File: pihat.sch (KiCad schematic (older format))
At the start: 1 part, among them J1 Raspberry_Pi_2_3

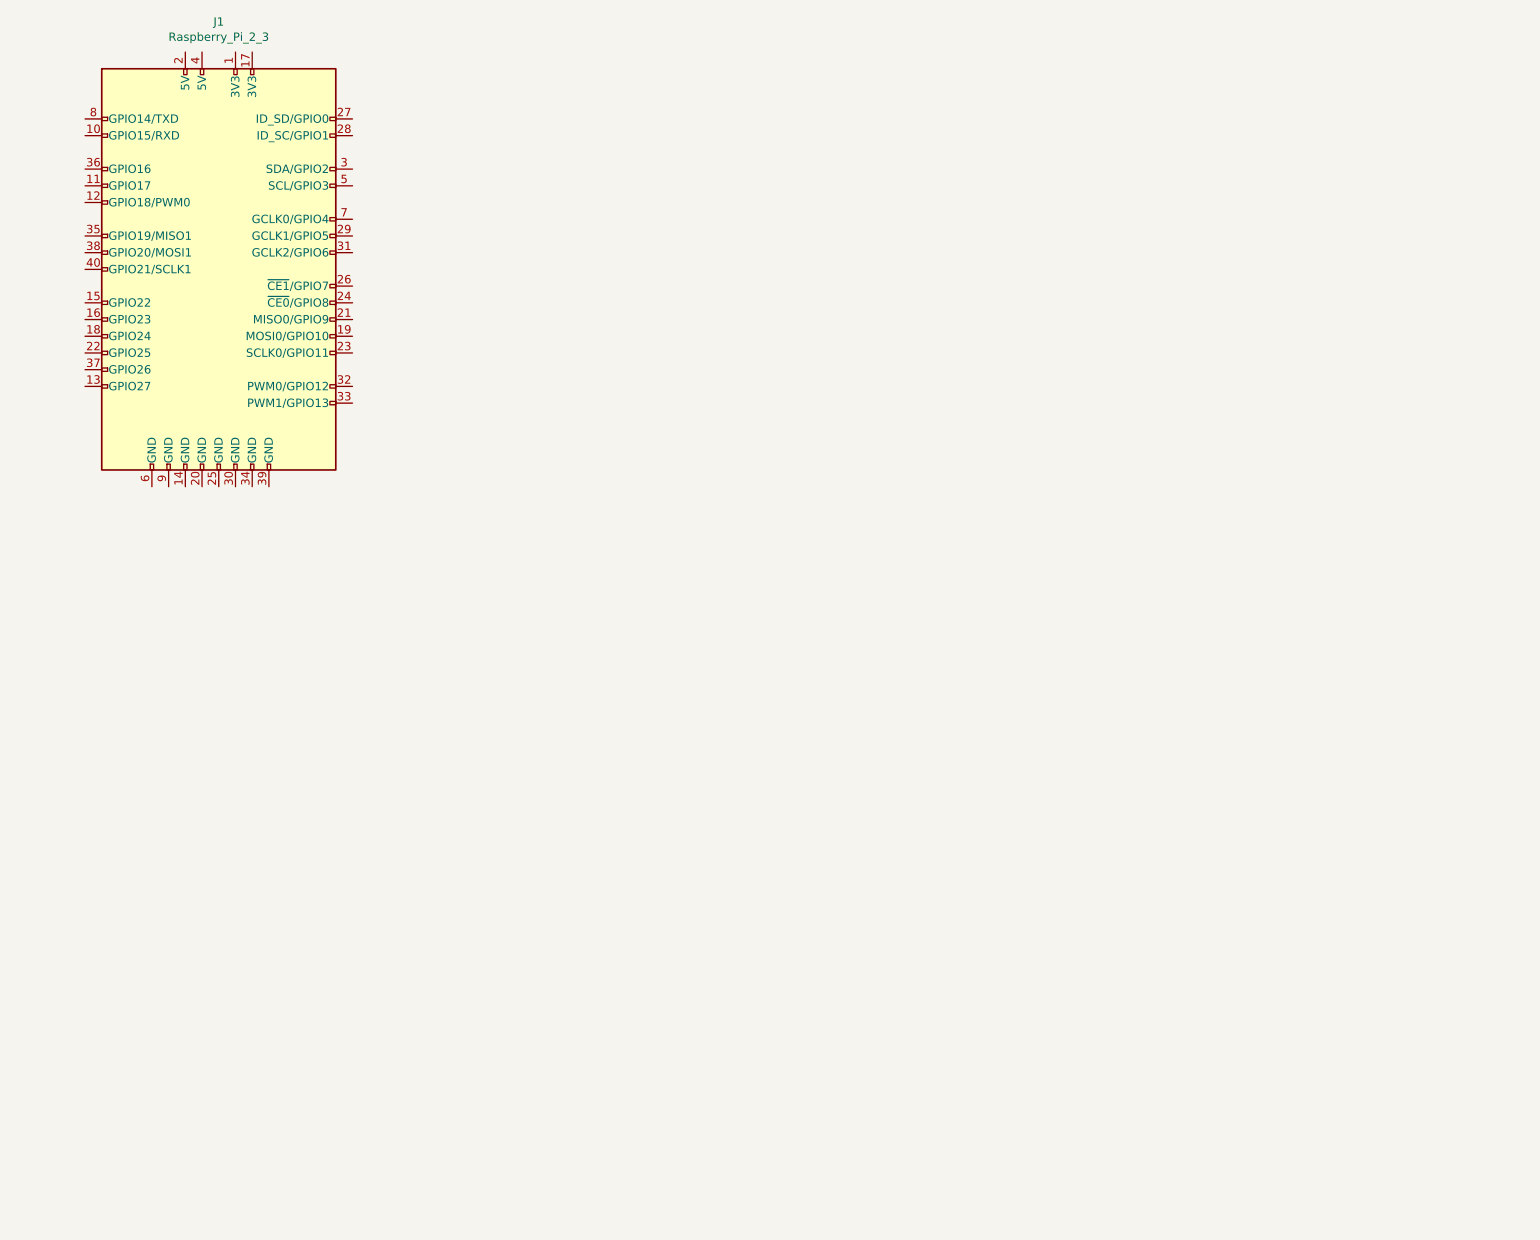
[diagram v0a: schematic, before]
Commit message: Add initial schematic for hat
This adds a USB<->UART converter and a 1-wire bus master, as well as
screw connectors for heating elements and sensors.
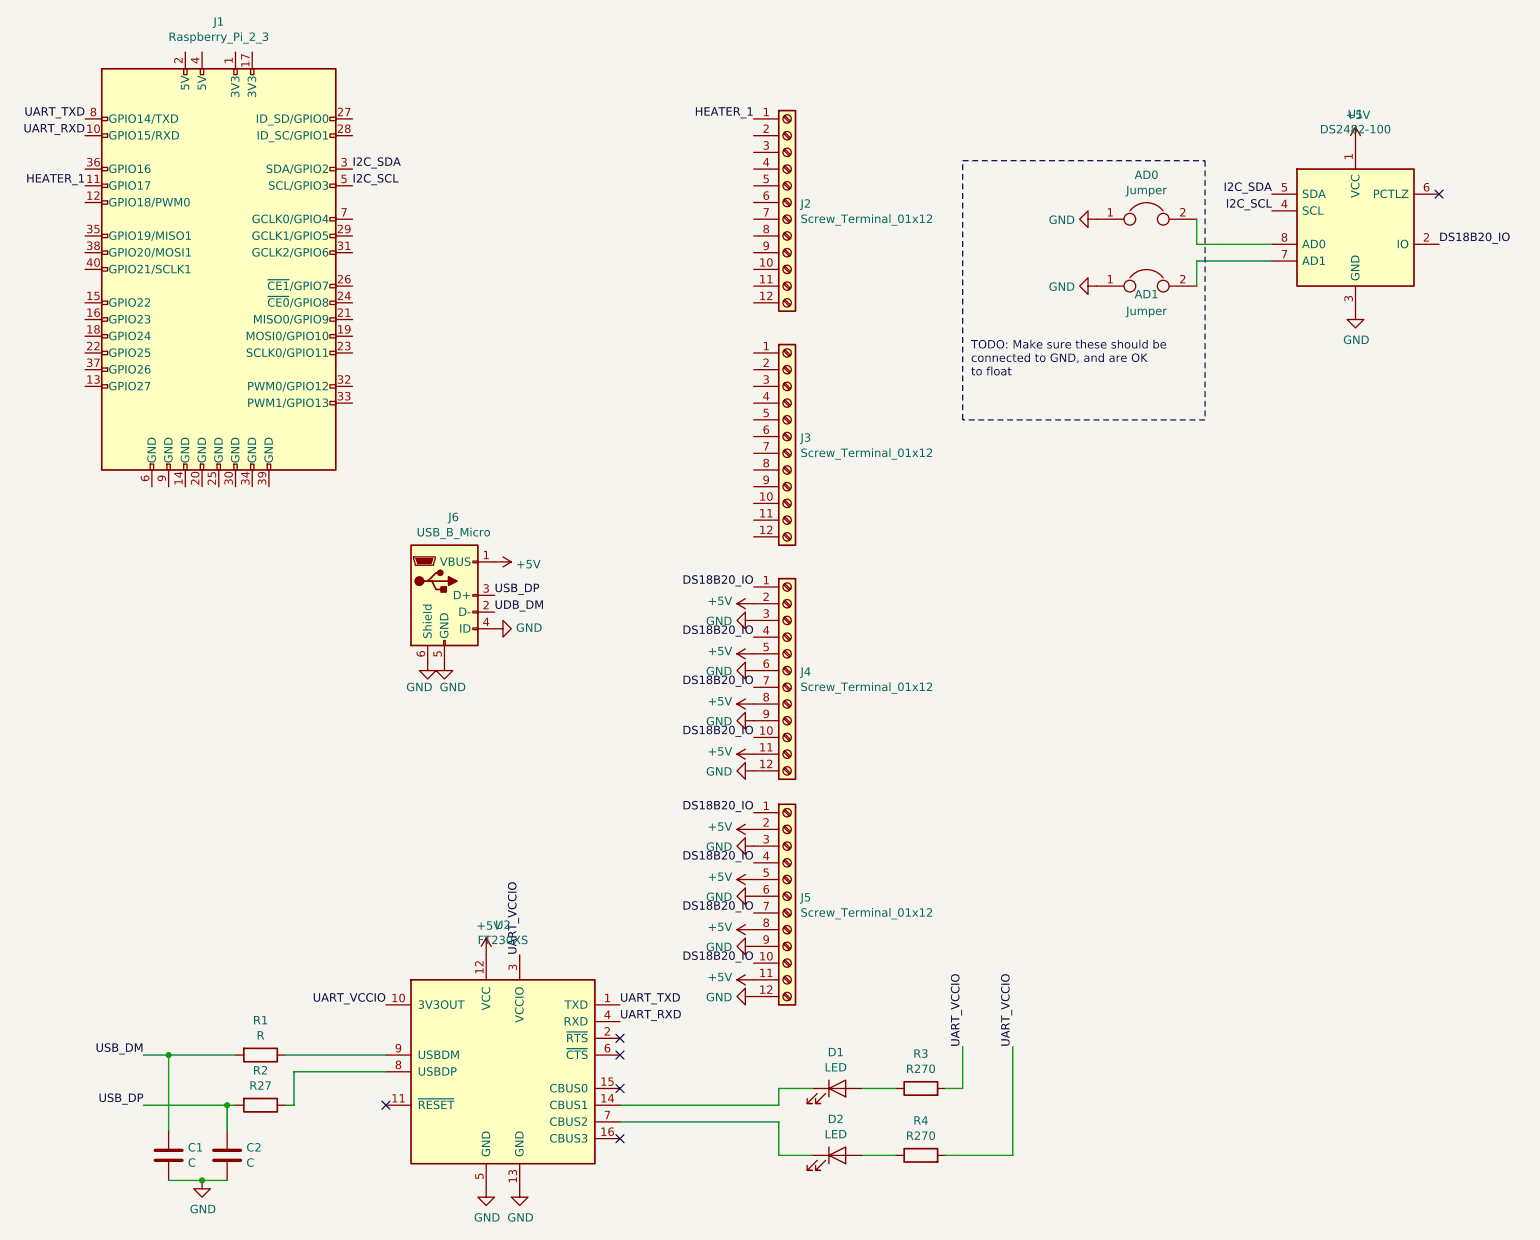
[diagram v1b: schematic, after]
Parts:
- added AD0, AD1: Jumper, Connector_PinHeader_2.54mm:PinHeader_1x02_P2.54mm_Vertical, symbol Device:Jumper
- added C1, C2: C, Capacitor_SMD:C_0603_1608Metric_Pad1.05x0.95mm_HandSolder, symbol Device:C
- added D1, D2: LED, LED_SMD:LED_0603_1608Metric_Pad1.05x0.95mm_HandSolder, symbol Device:LED
- added J2, J3, J4, J5: Screw_Terminal_01x12, TerminalBlock_Phoenix:TerminalBlock_Phoenix_MPT-0,5-12-2.54_1x12_P2.54mm_Horizontal, symbol Connector:Screw_Terminal_01x12
- added J6: USB_B_Micro, Connector_USB:USB_Micro-B_Wuerth_629105150521, symbol Connector:USB_B_Micro
- added R1: R, Resistor_SMD:R_0603_1608Metric_Pad1.05x0.95mm_HandSolder, symbol Device:R
- added R2: R27, Resistor_SMD:R_0603_1608Metric_Pad1.05x0.95mm_HandSolder, symbol Device:R
- added R3, R4: R270, Resistor_SMD:R_0603_1608Metric_Pad1.05x0.95mm_HandSolder, symbol Device:R
- added U1: DS2482-100, Package_SO:SOIC-8_3.9x4.9mm_P1.27mm, symbol maxim:DS2482-100
- added U2: FT230XS, Package_SO:SSOP-16_3.9x4.9mm_P0.635mm, symbol Interface_USB:FT230XS
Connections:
- net UART_RXD: now reaches J1.10 (GPIO15/RXD)
- net UART_RXD: now also U2.4 (RXD)
- net HEATER_1: now reaches J1.11 (GPIO17)
- net HEATER_1: now also J2.1 (Pin_1)
- net I2C_SDA: now reaches J1.3 (SDA/GPIO2)
- net I2C_SDA: now also U1.5 (SDA)
- net I2C_SCL: now reaches J1.5 (SCL/GPIO3)
- net I2C_SCL: now also U1.4 (SCL)
- net UART_TXD: now reaches J1.8 (GPIO14/TXD)
- net UART_TXD: now also U2.1 (TXD)
- new net: AD1.2, U1.7 (AD1)
- new net: AD0.2, U1.8 (AD0)
- new net: D1.1 (K), U2.14 (CBUS1)
- new net: D2.1 (K), U2.7 (CBUS2)
- new net: R2.1, U2.8 (USBDP)
- new net: R1.1, U2.9 (USBDM)
- new net: D1.2 (A), R3.1
- new net: D2.2 (A), R4.1
- new net +5V: J4.11 (Pin_11), J4.2 (Pin_2), J4.5 (Pin_5), J4.8 (Pin_8), J5.11 (Pin_11), J5.2 (Pin_2), J5.5 (Pin_5), J5.8 (Pin_8), J6.1 (VBUS), U1.1 (VCC), U2.12 (VCC)
- new net DS18B20_IO: J4.1 (Pin_1), J4.10 (Pin_10), J4.4 (Pin_4), J4.7 (Pin_7), J5.1 (Pin_1), J5.10 (Pin_10), J5.4 (Pin_4), J5.7 (Pin_7), U1.2 (IO)
- new net GND: AD0.1, AD1.1, C1.2, C2.2, J4.12 (Pin_12), J4.3 (Pin_3), J4.6 (Pin_6), J4.9 (Pin_9), J5.12 (Pin_12), J5.3 (Pin_3), J5.6 (Pin_6), J5.9 (Pin_9), J6.4 (ID), J6.5 (GND), J6.6 (Shield), U1.3 (GND), U2.13 (GND), U2.5 (GND)
- new net UART_VCCIO: R3.2, R4.2, U2.10 (3V3OUT), U2.3 (VCCIO)
- new net UDB_DM: J6.2 (D-)
- new net USB_DM: C1.1, R1.2
- new net USB_DP: C2.1, J6.3 (D+), R2.2
- no-connect marks 0 -> 6
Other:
- note added: "TODO: Make sure these should be\nconnected to GND, and are OK\nto float"
